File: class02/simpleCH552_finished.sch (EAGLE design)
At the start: 15 parts, among them U1 CH552G, X1 USBPCB

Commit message: remove fuse and test point
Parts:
- removed F1: DNP, adafruit:PTCFUSE-1206
- removed TP1, TP2: TEST-POINT3X4, SparkFun-Connectors:TEST-POINT3X4
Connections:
- net +5V: no longer F1.1, F1.2
- net USB_D+: no longer TP2.1
- net USB_D-: no longer TP1.1
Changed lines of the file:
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@@
 <attribute name="LCSC" value="C16834"/>
-</part>
-<part name="F1" library="adafruit" library_urn="urn:adsk.eagle:library:420" deviceset="PTCFUSE" device="-1206" value="DNP">
-<attribute name="LCSC" value="C151162"/>
 </part>
 <part name="GND1" library="SparkFun-PowerSymbols" library_urn="urn:adsk.eagle:library:530" deviceset="GND" device=""/>
@@
 <part name="P+4" library="supply1" library_urn="urn:adsk.eagle:library:371" deviceset="+5V" device=""/>
 <part name="P+5" library="supply1" library_urn="urn:adsk.eagle:library:371" deviceset="+5V" device=""/>
-<part name="TP1" library="SparkFun-Connectors" library_urn="urn:adsk.eagle:library:513" deviceset="TEST-POINT" device="3X4" package3d_urn="urn:adsk.eagle:package:38287/1"/>
-<part name="TP2" library="SparkFun-Connectors" library_urn="urn:adsk.eagle:library:513" deviceset="TEST-POINT" device="3X4" package3d_urn="urn:adsk.eagle:package:38287/1"/>
 <part name="S1" library="SparkFun-Switches" library_urn="urn:adsk.eagle:library:535" deviceset="MOMENTARY-SWITCH-SPST" device="-SMD-6.2MM-TALL" package3d_urn="urn:adsk.eagle:package:40172/1">
 <attribute name="LCSC" value="C557616"/>
@@
 <attribute name="VALUE" x="95.504" y="15.621" size="1.778" layer="96"/>
 </instance>
-<instance part="F1" gate="G$1" x="66.04" y="30.48" smashed="yes">
-<attribute name="LCSC" x="66.04" y="30.48" size="1.778" layer="96" display="off"/>
-<attribute name="NAME" x="62.23" y="35.56" size="1.778" layer="95"/>
-</instance>
 <instance part="GND1" gate="1" x="93.98" y="2.54" smashed="yes">
 <attribute name="VALUE" x="93.98" y="2.286" size="1.778" layer="96" align="top-center"/>
 </instance>
-<instance part="P+1" gate="1" x="73.66" y="38.1" smashed="yes">
-<attribute name="VALUE" x="71.12" y="40.64" size="1.778" layer="96"/>
+<instance part="P+1" gate="1" x="71.12" y="38.1" smashed="yes">
+<attribute name="VALUE" x="68.58" y="40.64" size="1.778" layer="96"/>
 </instance>
 <instance part="P+2" gate="1" x="93.98" y="30.48" smashed="yes">
@@
 <attribute name="LCSC" x="66.04" y="10.16" size="1.778" layer="96" rot="R90" display="off"/>
 </instance>
-<instance part="X1" gate="G$1" x="40.64" y="35.56" smashed="yes" rot="R180"/>
-<instance part="GND2" gate="1" x="43.18" y="43.18" smashed="yes" rot="R180">
-<attribute name="VALUE" x="45.72" y="45.72" size="1.778" layer="96" rot="R180"/>
+<instance part="X1" gate="G$1" x="48.26" y="35.56" smashed="yes" rot="R180"/>
+<instance part="GND2" gate="1" x="50.8" y="43.18" smashed="yes" rot="R180">
+<attribute name="VALUE" x="53.34" y="45.72" size="1.778" layer="96" rot="R180"/>
 </instance>
 <instance part="J1" gate="G$1" x="91.44" y="-20.32" smashed="yes">
@@
 <instance part="P+5" gate="1" x="73.66" y="22.86" smashed="yes">
 <attribute name="VALUE" x="76.2" y="22.86" size="1.778" layer="96"/>
-</instance>
-<instance part="TP1" gate="G$1" x="68.58" y="30.48" smashed="yes">
-<attribute name="NAME" x="73.66" y="30.48" size="1.778" layer="95" font="vector"/>
-</instance>
-<instance part="TP2" gate="G$1" x="68.58" y="27.94" smashed="yes">
-<attribute name="NAME" x="73.66" y="27.94" size="1.778" layer="95" font="vector"/>
 </instance>
 <instance part="S1" gate="G$1" x="66.04" y="20.32" smashed="yes">
@@
 <pinref part="X1" gate="G$1" pin="GND"/>
 <pinref part="GND2" gate="1" pin="GND"/>
-<wire x1="43.18" y1="35.56" x2="43.18" y2="40.64" width="0.1524" layer="91"/>
+<wire x1="50.8" y1="35.56" x2="50.8" y2="40.64" width="0.1524" layer="91"/>
 </segment>
 <segment>
@@
 <net name="USB_D-" class="0">
 <segment>
-<label x="53.34" y="30.48" size="1.778" layer="95"/>
+<label x="60.96" y="30.48" size="1.778" layer="95"/>
 <pinref part="X1" gate="G$1" pin="D-"/>
-<wire x1="68.58" y1="30.48" x2="43.18" y2="30.48" width="0.1524" layer="91"/>
-<pinref part="TP1" gate="G$1" pin="1"/>
+<wire x1="71.12" y1="30.48" x2="50.8" y2="30.48" width="0.1524" layer="91"/>
 </segment>
 <segment>
@@
 <net name="USB_D+" class="0">
 <segment>
-<label x="53.34" y="27.94" size="1.778" layer="95"/>
+<label x="60.96" y="27.94" size="1.778" layer="95"/>
 <pinref part="X1" gate="G$1" pin="D+"/>
-<wire x1="43.18" y1="27.94" x2="68.58" y2="27.94" width="0.1524" layer="91"/>
-<pinref part="TP2" gate="G$1" pin="1"/>
+<wire x1="50.8" y1="27.94" x2="71.12" y2="27.94" width="0.1524" layer="91"/>
 </segment>
 <segment>
@@
 <net name="+5V" class="0">
 <segment>
-<pinref part="F1" gate="G$1" pin="2"/>
-<wire x1="71.12" y1="33.02" x2="73.66" y2="33.02" width="0.1524" layer="91"/>
 <pinref part="P+1" gate="1" pin="+5V"/>
-<wire x1="73.66" y1="33.02" x2="73.66" y2="35.56" width="0.1524" layer="91"/>
 <wire x1="71.12" y1="33.02" x2="71.12" y2="35.56" width="0.1524" layer="91"/>
-<junction x="71.12" y="33.02"/>
-<wire x1="71.12" y1="35.56" x2="60.96" y2="35.56" width="0.1524" layer="91"/>
-<pinref part="F1" gate="G$1" pin="1"/>
 <pinref part="X1" gate="G$1" pin="VBUS"/>
-<wire x1="43.18" y1="33.02" x2="60.96" y2="33.02" width="0.1524" layer="91"/>
-<wire x1="60.96" y1="35.56" x2="60.96" y2="33.02" width="0.1524" layer="91"/>
-<junction x="60.96" y="33.02"/>
-</segment>
-<segment>
+<wire x1="50.8" y1="33.02" x2="71.12" y2="33.02" width="0.1524" layer="91"/>
+</segment>
+<segment>

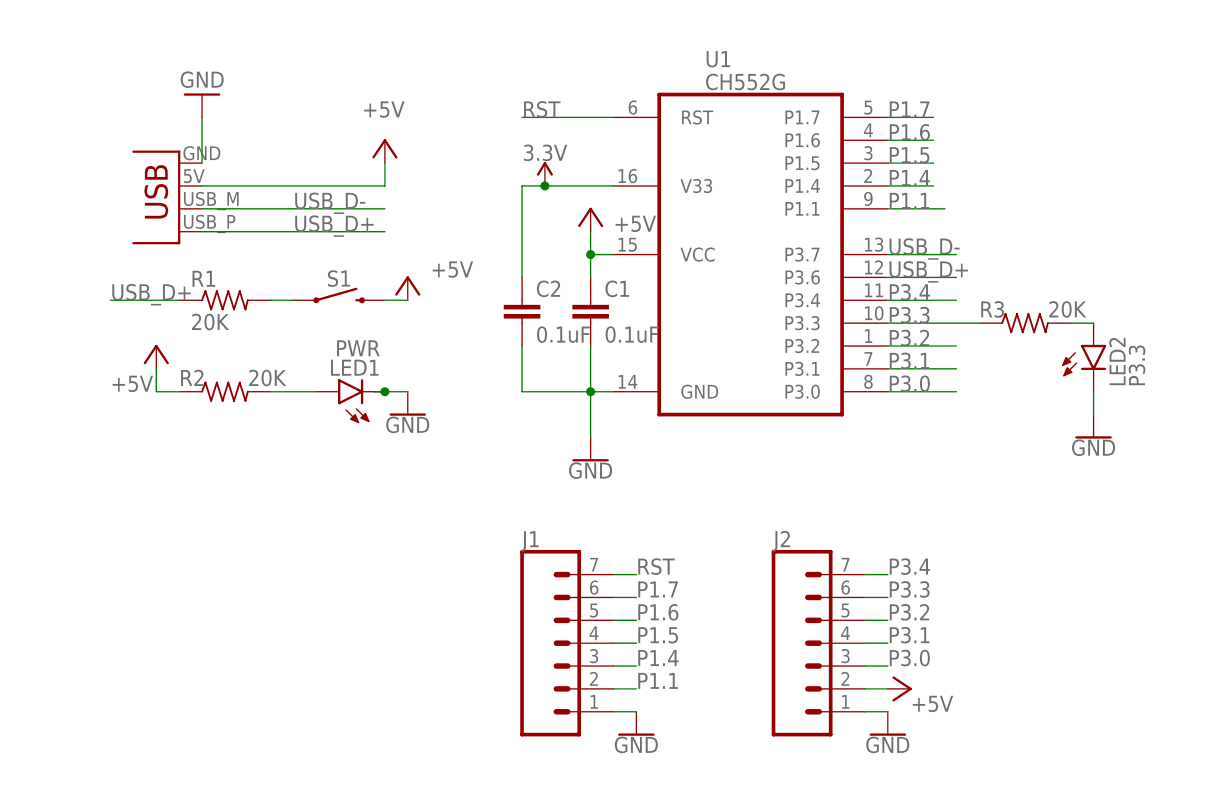
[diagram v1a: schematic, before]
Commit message: update to USB shell model
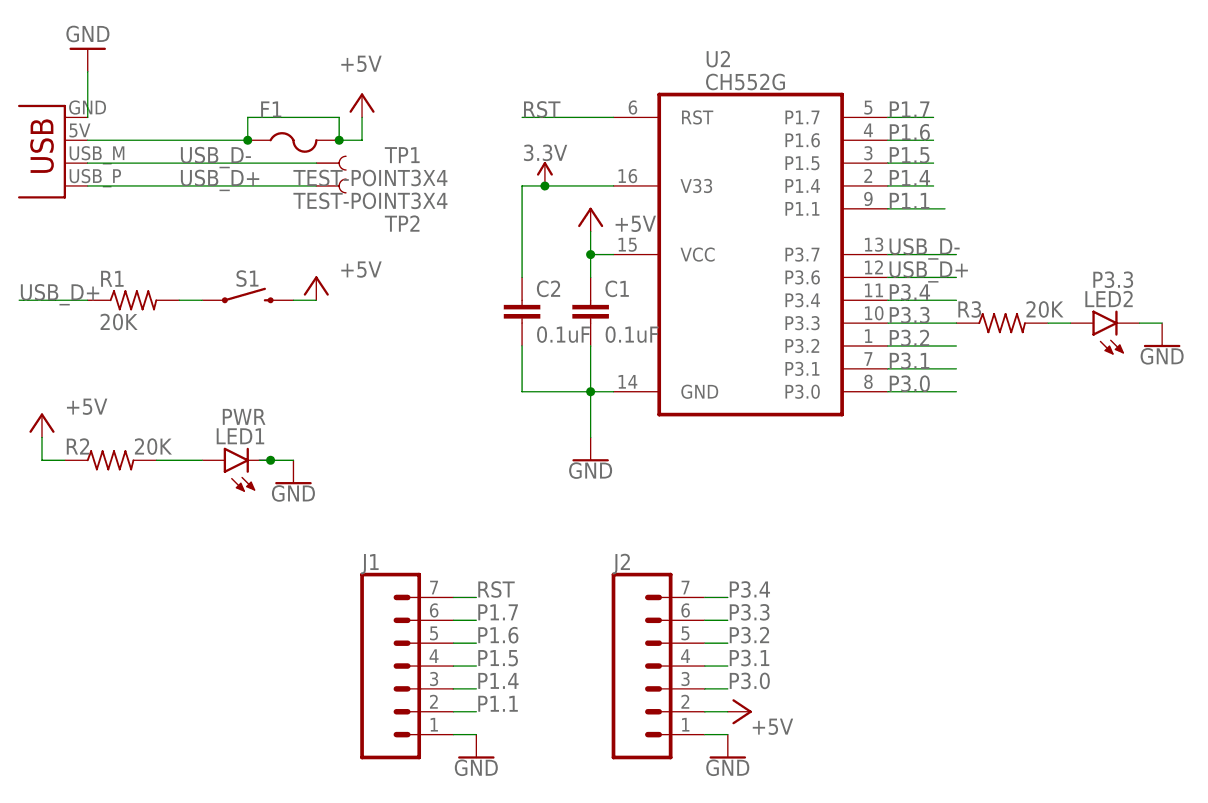
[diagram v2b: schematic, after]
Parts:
- added F1: (no value), adafruit:PTCFUSE-1206
- added TP1, TP2: TEST-POINT3X4, SparkFun-Connectors:TEST-POINT3X4
- LED1: LCSC C389523 -> (none)
- LED2: LCSC C389524 -> (none)
- R1, R2, R3: LCSC C702832 -> (none)
- S1: LCSC C557616 -> (none)
- renumbered U1 to U2
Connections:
- net +5V: now also F1.1, F1.2
- net USB_D+: now also TP2.1
- net USB_D-: now also TP1.1
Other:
- moved on the sheet: J1, J2, LED1, LED2, R1, R2, R3, S1
